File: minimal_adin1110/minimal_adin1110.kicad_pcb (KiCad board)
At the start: 4 copper layers, 27 x 21.4 mm, 32 parts, among them U6 ADIN1110CCPZ, Y1 FA-128 25.0000MF20X-K0

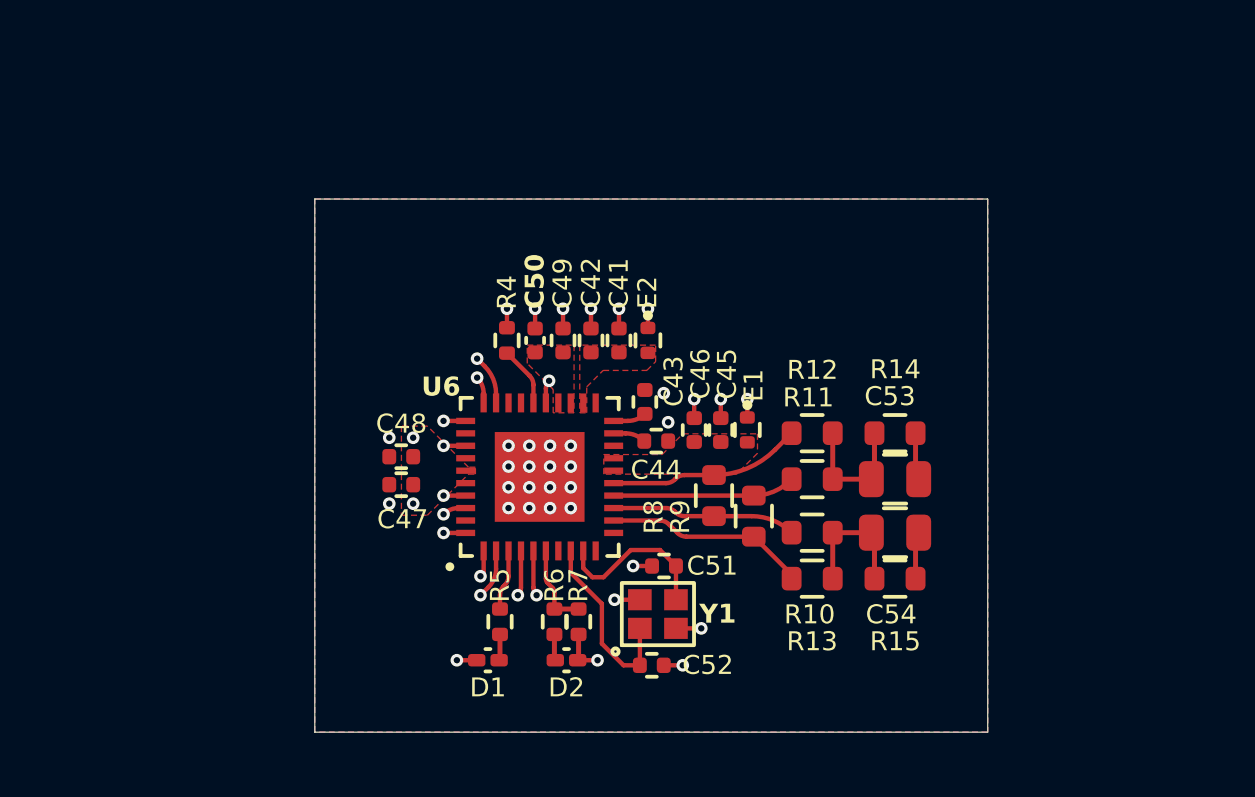
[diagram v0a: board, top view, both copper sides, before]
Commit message: Add VRML file reference for minimal_adin1110 project
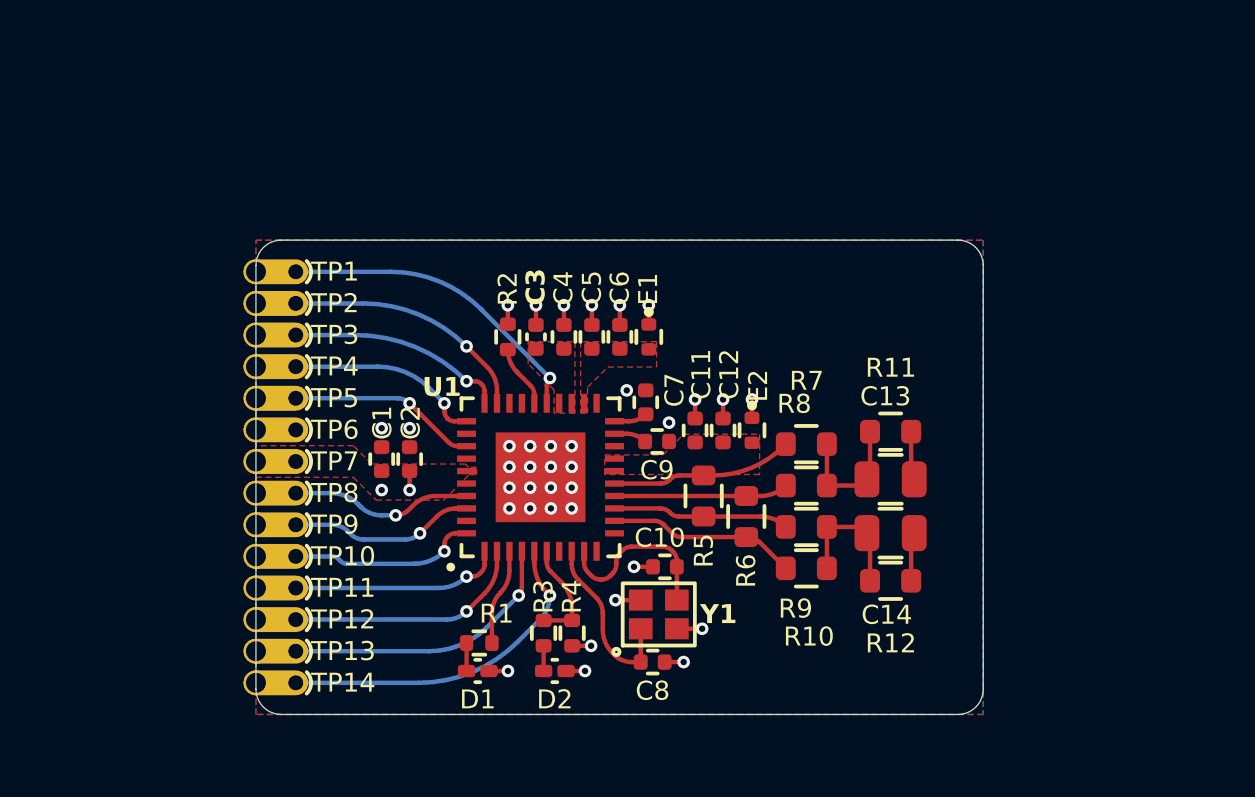
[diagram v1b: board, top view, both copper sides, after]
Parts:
- added TP1: TestPoint, test_point_footprints:TestPoint_THTPad_Castelated, F.Cu at (120.4, 78.9)
- added TP10: TestPoint, test_point_footprints:TestPoint_THTPad_Castelated, F.Cu at (120.4, 90.3)
- added TP11: TestPoint, test_point_footprints:TestPoint_THTPad_Castelated, F.Cu at (120.4, 91.6)
- added TP12: TestPoint, test_point_footprints:TestPoint_THTPad_Castelated, F.Cu at (120.4, 92.8)
- added TP13: TestPoint, test_point_footprints:TestPoint_THTPad_Castelated, F.Cu at (120.4, 94.1)
- added TP14: TestPoint, test_point_footprints:TestPoint_THTPad_Castelated, F.Cu at (120.4, 95.4)
- added TP2: TestPoint, test_point_footprints:TestPoint_THTPad_Castelated, F.Cu at (120.4, 80.1)
- added TP3: TestPoint, test_point_footprints:TestPoint_THTPad_Castelated, F.Cu at (120.4, 81.4)
- added TP4: TestPoint, test_point_footprints:TestPoint_THTPad_Castelated, F.Cu at (120.4, 82.7)
- added TP5: TestPoint, test_point_footprints:TestPoint_THTPad_Castelated, F.Cu at (120.4, 83.9)
- added TP6: TestPoint, test_point_footprints:TestPoint_THTPad_Castelated, F.Cu at (120.4, 85.2)
- added TP7: TestPoint, test_point_footprints:TestPoint_THTPad_Castelated, F.Cu at (120.4, 86.5)
- added TP8: TestPoint, test_point_footprints:TestPoint_THTPad_Castelated, F.Cu at (120.4, 87.8)
- added TP9: TestPoint, test_point_footprints:TestPoint_THTPad_Castelated, F.Cu at (120.4, 89.0)
- moved C1 1.29 mm to (125.4, 86.4), turned to 90 degrees
- moved R1 1.19 mm to (129.4, 93.8), turned to 0 degrees
- moved D2 0.64 mm to (132.4, 94.9)
- moved R3 0.63 mm to (131.9, 93.4)
- moved D1 0.59 mm to (129.3, 94.9), turned to 0 degrees
- moved R4 0.53 mm to (133.1, 93.4)
- moved R7 0.50 mm to (142.5, 85.8)
- moved R10 0.48 mm to (142.5, 90.8)
- moved R5 0.42 mm to (138.4, 87.9)
- moved C2 0.35 mm to (126.6, 86.4), turned to 90 degrees
- moved R8 0.35 mm to (142.5, 87.5)
- moved R9 0.33 mm to (142.5, 89.1)
- moved R6 0.30 mm to (140.1, 88.7)
- moved R12 0.20 mm to (145.9, 91.3)
- moved E2 0.19 mm to (140.3, 85.2)
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- renumbered C47 to C1, C51 to C10, C46 to C11, C45 to C12, C53 to C13, C54 to C14, C48 to C2, C50 to C3, C49 to C4, C42 to C5, C41 to C6, C43 to C7, C52 to C8, C44 to C9, E2 to E1, E1 to E2, R5 to R1, R13 to R10, R14 to R11, R15 to R12, R4 to R2, R6 to R3, R7 to R4, R8 to R5, R9 to R6, R12 to R7, R11 to R8, R10 to R9, U6 to U1
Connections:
- C1 pad 1: /3V3 -> /VDDIO
- C2 pad 1: /3V3 -> /VDDIO
- D1 pad 2: /3V3 -> /VDDIO
- D2 pad 2: /3V3 -> /VDDIO
- R4 pad 1: /3V3 -> /VDDIO
- U1 pad 25: /INT -> /~{INT}
- U1 pad 29: /SS3 -> /~{CS}
- U1 pad 31: /TX2P4_EN -> /~{TX2P4_EN}
- U1 pad 33: /SWPD_EN -> /~{SWPD_EN}
- U1 pad 35: /3V3 -> /VDDIO
- U1 pad 5: /RESET -> /~{RESET}
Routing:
- net /~{RESET}: track 0.00 -> 13.6 mm, vias 0 -> 1
- net /~{INT}: track 0.00 -> 12.8 mm, vias 0 -> 1
- net /~{CS}: track 0.00 -> 10.0 mm, vias 0 -> 1
- net /LINK_ST: track 1.81 -> 11.5 mm
- net /~{TX2P4_EN}: track 0.00 -> 7.87 mm, vias 0 -> 1
- net /MISO: track 1.99 -> 9.78 mm
- net /TS_TIMER__MS_SEL: track 1.08 -> 8.76 mm
- net /~{SWPD_EN}: track 0.00 -> 7.60 mm, vias 0 -> 1
- net /MOSI: track 1.07 -> 8.49 mm
- net /TS_CAPT: track 0.89 -> 7.60 mm
- net /SCK: track 0.95 -> 7.45 mm
- net /SPI_CFG1: track 0.89 -> 7.32 mm
- net /VDDIO: track 0.00 -> 3.05 mm, vias 0 -> 5
- net /3V3: track 4.85 -> 2.29 mm, vias 7 -> 3
- net /SS3: track 2.02 -> 0.00 mm, vias 1 -> 0
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- added copper zone on F.Cu, net /VDDIO
- added copper zone on In1.Cu, net /VDDIO
- removed copper zone on F.Cu, net /3V3
- removed copper zone on In1.Cu, net /3V3
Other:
- board size 27 x 21.4 mm -> 29.2 x 19.1 mm

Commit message: Backup
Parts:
- added J1: CLP-102-02-G-D-BE, connector_footprints:CLP-102-02-G-D-BE, F.Cu at (145.2, 73.2)
- added J2: CLP-102-02-G-D-BE, connector_footprints:CLP-102-02-G-D-BE, F.Cu at (138.8, 73.2)
- added J3: CLP-102-02-G-D-BE, connector_footprints:CLP-102-02-G-D-BE, F.Cu at (128.7, 73.2)
- added J4: CLP-112-02-G-D-BE, connector_footprints:CLP-114-02-G-D-BE, F.Cu at (116.0, 87.1)
- added JP1: SolderJumper_3_Open, solder_jumper_footprints:SolderJumper-3_P1.3mm_Open_RoundedPad1.0x1.5mm_NumberLabels, F.Cu at (141.2, 79.1)
- added JP2: SolderJumper_3_Open, solder_jumper_footprints:SolderJumper-3_P1.3mm_Open_RoundedPad1.0x1.5mm_NumberLabels, F.Cu at (147.6, 79.1)
- added JP3: SolderJumper_3_Open, solder_jumper_footprints:SolderJumper-3_P1.3mm_Open_RoundedPad1.0x1.5mm_NumberLabels, F.Cu at (132.2, 78.1)
- added REF**: mouse-bite-50mil-790mil, mouse_bite_footprints:mouse-bite-50mil-790mil, F.Cu at (119.9, 87.1)
- added REF**: mouse-bite-midle-50mil-200mil, mouse_bite_footprints:mouse-bite-midle-50mil-200mil, F.Cu at (128.7, 75.7)
- added REF**: mouse-bite-midle-50mil-200mil, mouse_bite_footprints:mouse-bite-midle-50mil-200mil, F.Cu at (138.8, 75.7)
- added REF**: mouse-bite-midle-50mil-200mil, mouse_bite_footprints:mouse-bite-midle-50mil-200mil, F.Cu at (145.2, 75.7)
- added TP15: TestPoint, test_point_footprints:TestPoint_THTPad_Castelated, F.Cu at (145.8, 76.3)
- added TP16: TestPoint, test_point_footprints:TestPoint_THTPad_Castelated, F.Cu at (139.4, 76.3)
- added TP17: TestPoint, test_point_footprints:TestPoint_THTPad_Castelated, F.Cu at (138.2, 76.3)
- added TP18: TestPoint, test_point_footprints:TestPoint_THTPad_Castelated, F.Cu at (144.5, 76.3)
- added TP19: TestPoint, test_point_footprints:TestPoint_THTPad_Castelated, F.Cu at (129.3, 76.3)
- added TP20: TestPoint, test_point_footprints:TestPoint_THTPad_Castelated, F.Cu at (128.0, 76.3)
- moved E2 2.54 mm to (138.7, 83.3), turned to 180 degrees
- moved E1 1.94 mm to (138.0, 80.8), turned to 180 degrees
- moved C5 1.34 mm to (135.1, 80.8)
- moved C6 1.34 mm to (136.2, 80.8)
- moved C3 0.89 mm to (132.3, 80.8)
- moved C4 0.89 mm to (133.4, 80.8)
- moved C12 0.87 mm to (138.7, 84.5), turned to 0 degrees
- moved C11 0.79 mm to (138.7, 85.7), turned to 0 degrees
- moved R2 0.37 mm to (130.2, 81.6)
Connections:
- C3 pad 1: /DLDO_1P1 -> /DVDD_1P1
- E1 pad 1: /3V3 -> /AVDD_L_IN
- E2 pad 1: /3V3 -> /AVDD_H_IN
- R2 pad 1: /3V3 -> /VDDIO
- U1 pad 24: /DLDO_1P1 -> /DVDD_1P1
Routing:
- net /~{RESET}: track 13.6 -> 16.2 mm
- net /LINK_ST: track 11.5 -> 14.1 mm
- net /MISO: track 9.78 -> 12.4 mm
- net /MOSI: track 8.49 -> 11.1 mm
- net /TS_CAPT: track 7.60 -> 10.2 mm
- net /~{TX2P4_EN}: track 7.87 -> 10.5 mm
- net /TS_TIMER__MS_SEL: track 8.76 -> 11.3 mm
- net /SPI_CFG1: track 7.32 -> 9.90 mm
- net /SCK: track 7.45 -> 10.0 mm
- net /~{SWPD_EN}: track 7.60 -> 10.2 mm
- net /~{CS}: track 10.0 -> 12.6 mm
- net /3V3: track 2.29 -> 0.00 mm, vias 3 -> 0
- net /~{INT}: track 12.8 -> 15.0 mm
- net /VDDIO: track 3.05 -> 3.78 mm, vias 5 -> 10
- added copper zone on F.Cu, net /1P1_EXT
- added copper zone on F.Cu, net /AVDD_H_EXT
- added copper zone on F.Cu, net /AVDD_H_IN
- added copper zone on F.Cu, net /AVDD_L_EXT
- added copper zone on F.Cu, net /AVDD_L_IN
- added copper zone on F.Cu, net /DVDD_1P1
- added copper zone on In1.Cu, net GND
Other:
- board size 29.2 x 19.1 mm -> 40 x 27.9 mm

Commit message: Backup
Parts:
- added J5: CLP-102-02-G-D-BE, connector_footprints:CLP-102-02-G-D-BE, F.Cu at (152.8, 88.4)
- added REF**: mouse-bite-midle-50mil-200mil, mouse_bite_footprints:mouse-bite-midle-50mil-200mil, F.Cu at (150.2, 88.4)
- added TP21: TestPoint, test_point_footprints:TestPoint_THTPad_Castelated, F.Cu at (149.6, 87.8)
- added TP22: TestPoint, test_point_footprints:TestPoint_THTPad_Castelated, F.Cu at (149.6, 89.0)
- C3: value 0.68uF -> 680 nF; footprint footprints:C_0402_1005Metric -> capacitor_footprints:C_0402_1005Metric
- moved C13 0.79 mm to (145.1, 87.3)
- moved C14 0.79 mm to (145.1, 89.5)
- moved R7 0.79 mm to (141.7, 85.9)
- moved R8 0.79 mm to (141.7, 87.6)
- moved R9 0.79 mm to (141.7, 89.2)
- moved R10 0.79 mm to (141.7, 90.9)
- moved R11 0.79 mm to (145.1, 85.4)
- moved R12 0.79 mm to (145.1, 91.4)
- moved R5 0.78 mm to (137.6, 87.9)
- moved R6 0.78 mm to (139.3, 88.7)
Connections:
- net Net-(C13-Pad1) renamed /DATA_AND_POWER_P
- net Net-(C14-Pad1) renamed /DATA_AND_POWER_N
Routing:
- net /DATA_AND_POWER_N: track 1.97 -> 8.20 mm
- net /DATA_AND_POWER_P: track 1.97 -> 8.20 mm
- net /TXP: track 7.29 -> 6.17 mm
- net /RXP: track 6.98 -> 6.22 mm
- net /TXN: track 7.58 -> 6.93 mm
- net /RXN: track 7.07 -> 6.45 mm
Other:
- board size 40 x 27.9 mm -> 43.2 x 27.9 mm

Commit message: Add UNITED_MOUSE_BITES_DATA_BASE library to sym-lib-table
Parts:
- removed REF**: mouse-bite-50mil-790mil, mouse_bite_footprints:mouse-bite-50mil-790mil
- removed REF** (x4): mouse-bite-midle-50mil-200mil, mouse_bite_footprints:mouse-bite-midle-50mil-200mil
- added MB1: mouse-bite-midle-50mil-200mil, mouse_bite_footprints:mouse-bite-50mil-790mil, F.Cu at (119.9, 87.1)
- added MB2: mouse-bite-midle-50mil-200mil, mouse_bite_footprints:mouse-bite-midle-50mil-200mil, F.Cu at (128.7, 75.7)
- added MB3: mouse-bite-midle-50mil-200mil, mouse_bite_footprints:mouse-bite-midle-50mil-200mil, F.Cu at (138.8, 75.7)
- added MB4: mouse-bite-midle-50mil-200mil, mouse_bite_footprints:mouse-bite-midle-50mil-200mil, F.Cu at (145.2, 75.7)
- added MB5: mouse-bite-midle-50mil-200mil, mouse_bite_footprints:mouse-bite-midle-50mil-200mil, F.Cu at (150.2, 88.4)
- renumbered C12 to C11, C11 to C12, C7 to C6, C6 to C7, J4 to J1, J3 to J2, J2 to J3, J1 to J4, JP3 to JP1, JP1 to JP2, JP2 to JP3, TP20 to TP15, TP19 to TP16, TP16 to TP18, TP18 to TP19, TP15 to TP20

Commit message: Minor changes
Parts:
- moved J3 1.27 mm to (137.5, 73.2)
- moved MB3 1.27 mm to (137.5, 75.7)
- moved TP18 1.27 mm to (138.2, 76.3)
- moved TP17 1.27 mm to (136.9, 76.3)
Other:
- outline, holes or cut-outs redrawn

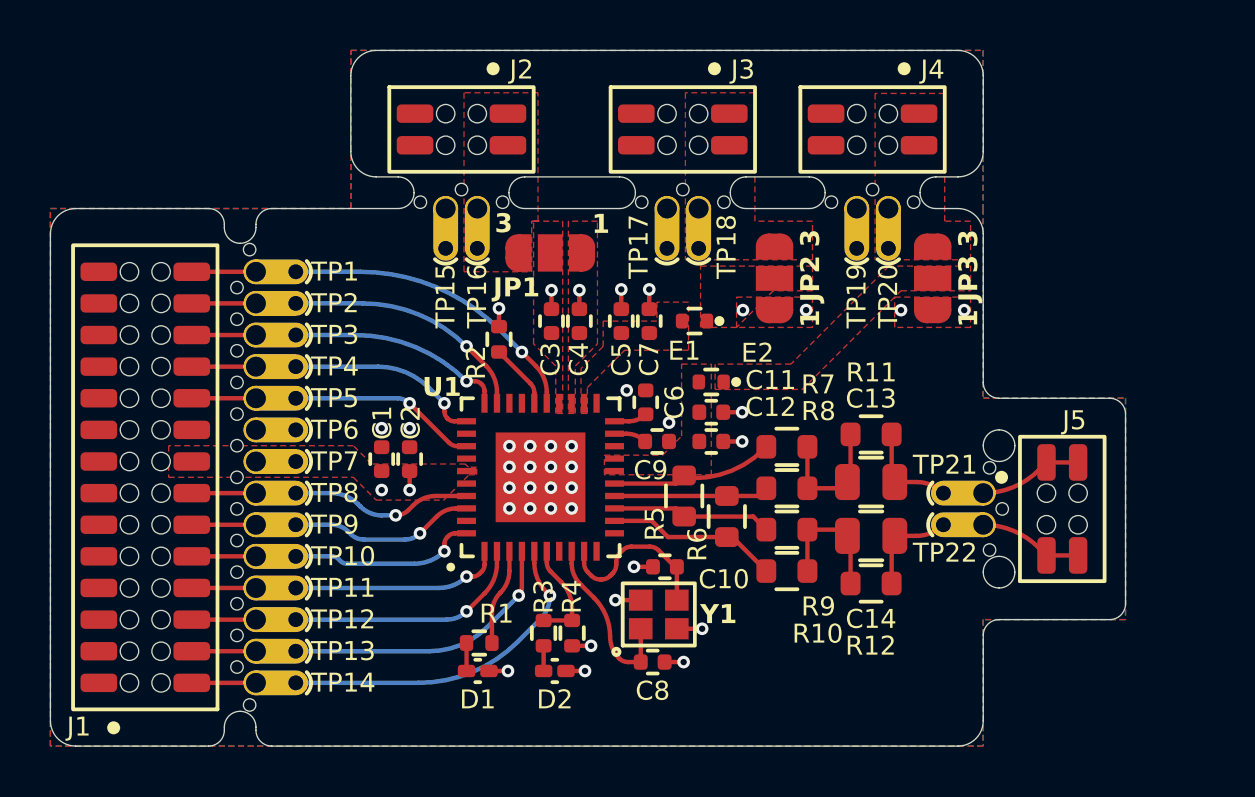
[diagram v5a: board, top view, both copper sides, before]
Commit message: Update component blacklist and add new libraries to symbol and footprint tables
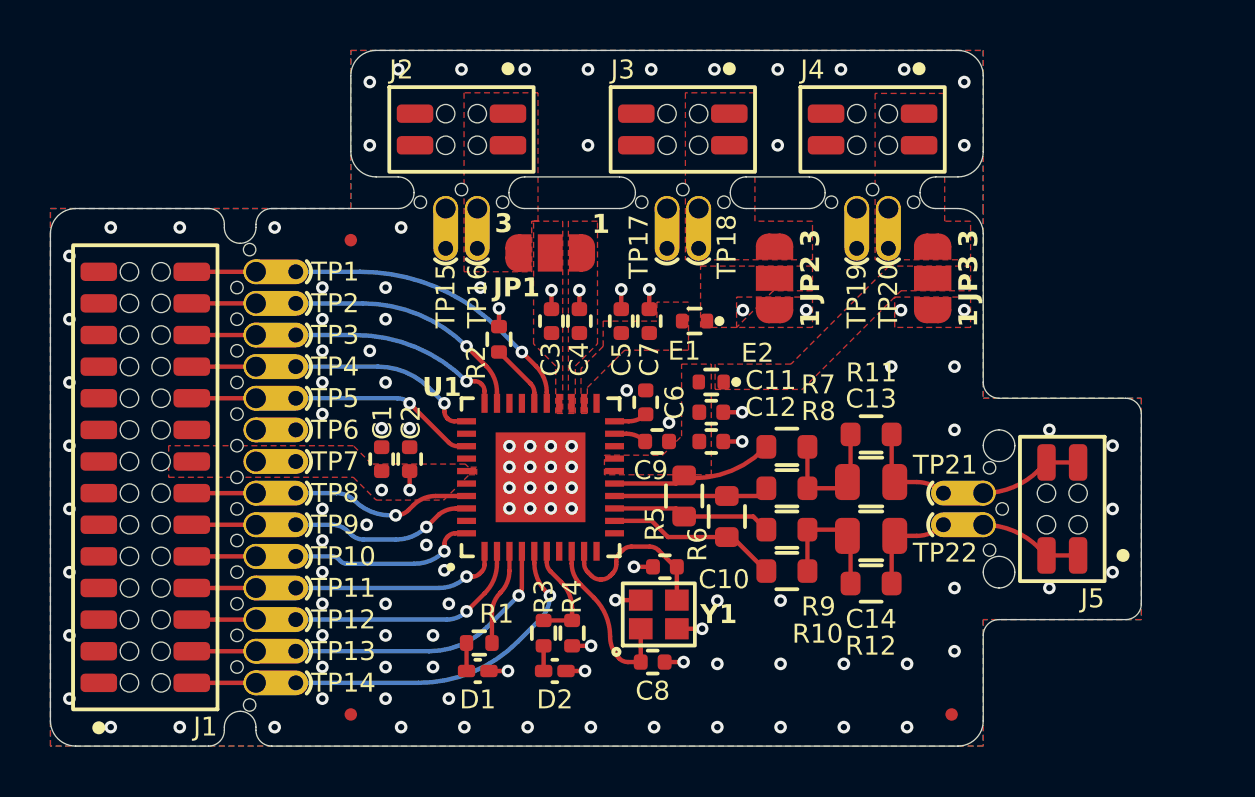
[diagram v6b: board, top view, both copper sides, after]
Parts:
- added FID1: Fiducial, no_components_footprints:Fiducial_0.5mm_Mask1mm, F.Cu at (124.2, 77.6)
- added FID2: Fiducial, no_components_footprints:Fiducial_0.5mm_Mask1mm, F.Cu at (124.2, 96.6)
- added FID3: Fiducial, no_components_footprints:Fiducial_0.5mm_Mask1mm, F.Cu at (148.3, 96.6)
- turned J5 to 180 degrees
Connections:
- J5 pad 1: /DATA_AND_POWER_P -> /DATA_AND_POWER_N
- J5 pad 2: /DATA_AND_POWER_N -> /DATA_AND_POWER_P
- J5 pad 3: /DATA_AND_POWER_P -> /DATA_AND_POWER_N
- J5 pad 4: /DATA_AND_POWER_N -> /DATA_AND_POWER_P
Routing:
- net GND: vias 30 -> 113
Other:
- board size 43.2 x 27.9 mm -> 43.8 x 27.9 mm

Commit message: Update subproject commit for KiCAD Symbol Generator
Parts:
- moved C14 2.87 mm to (146.5, 92.0)
- moved R12 2.87 mm to (146.5, 93.9)
- moved R6 1.76 mm to (140.7, 89.8)
- moved R10 1.76 mm to (143.1, 92.0)
- moved R5 1.76 mm to (139.0, 89.0)
- moved R7 1.76 mm to (143.1, 87.0)
- moved R8 1.76 mm to (143.1, 88.7)
- moved R9 1.76 mm to (143.1, 90.3)
- moved C13 1.40 mm to (146.5, 87.0)
- moved R11 1.40 mm to (146.5, 85.1)
- moved J5 1.27 mm to (153.4, 89.5), turned to 90 degrees
- moved MB5 1.12 mm to (150.2, 89.5)
- moved TP21 1.11 mm to (149.6, 88.9)
- moved TP22 1.11 mm to (149.6, 90.1)
- moved TP17 0.64 mm to (136.3, 76.3)
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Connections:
- J5 pad 2: /DATA_AND_POWER_P -> GND
- J5 pad 3: /DATA_AND_POWER_N -> /DATA_AND_POWER_P
- J5 pad 4: /DATA_AND_POWER_P -> GND
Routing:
- net /DATA_AND_POWER_P: track 8.20 -> 5.89 mm
- net /DATA_AND_POWER_N: track 8.20 -> 5.89 mm
- net /TXP: track 6.17 -> 7.95 mm
- net /TXN: track 6.93 -> 8.58 mm
- net /RXP: track 6.22 -> 7.82 mm
- net /RXN: track 6.45 -> 8.01 mm
- net GND: vias 113 -> 125
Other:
- board size 43.8 x 27.9 mm -> 45.1 x 27.9 mm
